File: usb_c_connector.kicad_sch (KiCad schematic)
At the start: 24 parts, among them J4 USB_C_Receptacle_USB2.0_16P, J5 USB_C_Receptacle_USB2.0_16P, U6 LM66100DCK, U7 LM66100DCK, U8 USBLC6-2SC6, U9 USBLC6-2SC6

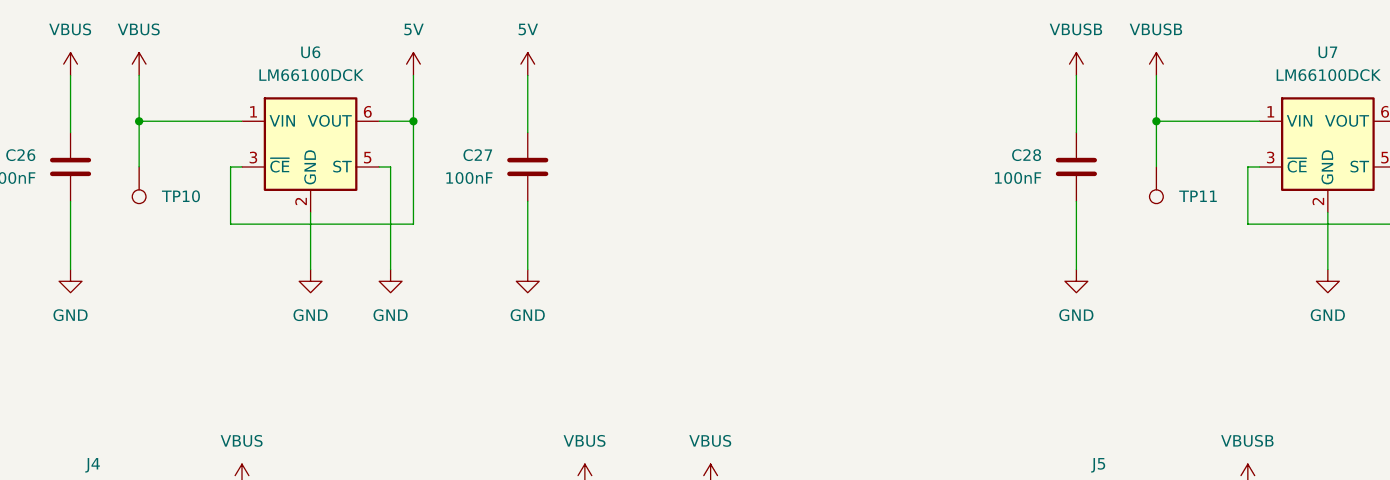
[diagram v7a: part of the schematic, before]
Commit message: Move fuse to correct location
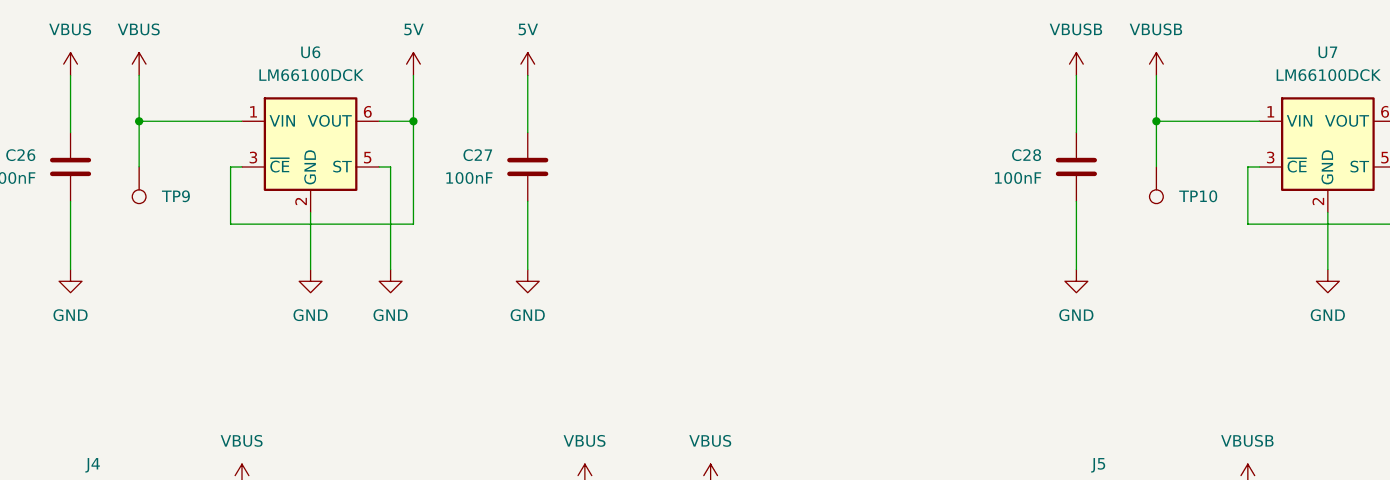
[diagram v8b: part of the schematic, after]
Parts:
- renumbered TP11 to TP10, TP10 to TP9
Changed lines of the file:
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@@
 		(dnp no)
 		(fields_autoplaced yes)
-		(property "Reference" "TP10"
+		(property "Reference" "TP9"
 			(at 74.93 57.9119 0)
 			(effects
@@
 			(project "Tumbler2_Redesign"
 				(path "/f3fd8d79-9d35-4c04-811e-2697a2740958/84b20f1f-6e00-4937-92e5-6e005c1bde3e"
-					(reference "TP10")
+					(reference "TP9")
 					(unit 1)
 				)
@@
 		(dnp no)
 		(fields_autoplaced yes)
-		(property "Reference" "TP11"
+		(property "Reference" "TP10"
 			(at 187.96 57.9119 0)
 			(effects
@@
 			(project "Tumbler2_Redesign"
 				(path "/f3fd8d79-9d35-4c04-811e-2697a2740958/84b20f1f-6e00-4937-92e5-6e005c1bde3e"
-					(reference "TP11")
-					(unit 1)
-				)
+					(reference "TP10")
+					(unit 1)
+				)
